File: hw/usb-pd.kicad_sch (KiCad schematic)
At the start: 16 parts, among them J2101 USB C power only, Q2101 SQJ433EP, U2103 STUSB4500QTR

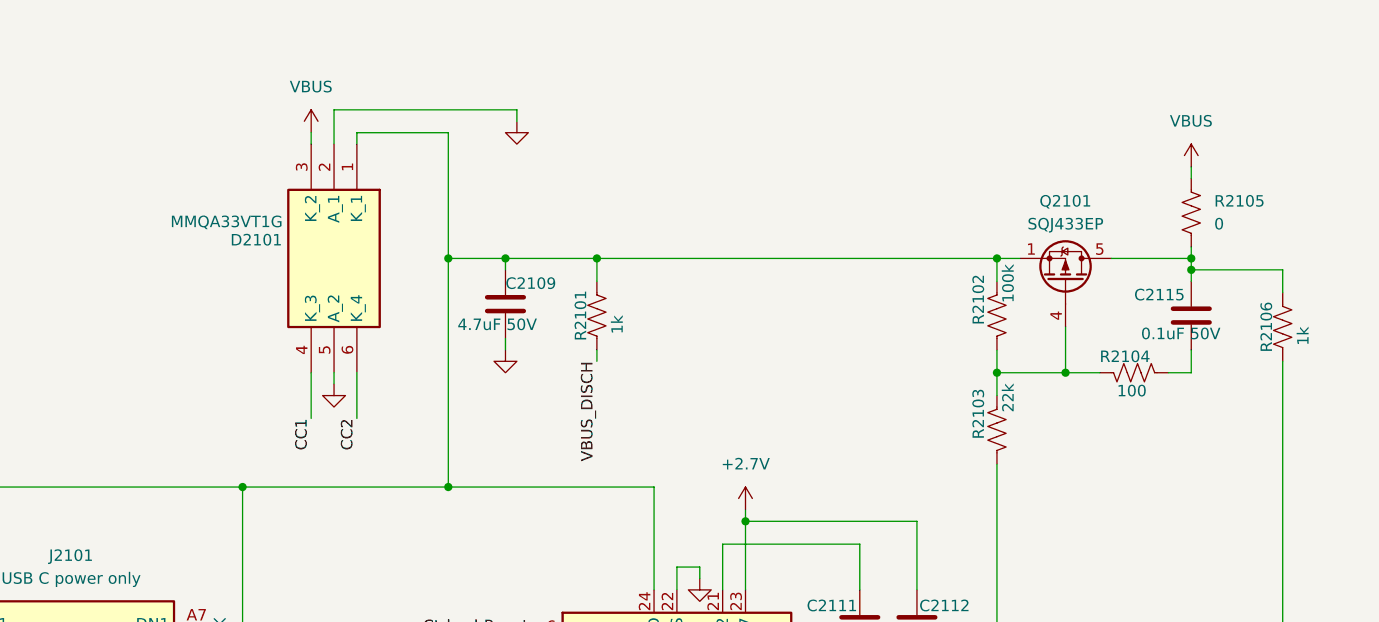
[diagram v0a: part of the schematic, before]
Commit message: I laid down three QSDs but have not done any canyon for 800 ohm yet. Starting to look at Veer buck/boost to round out my understanding.
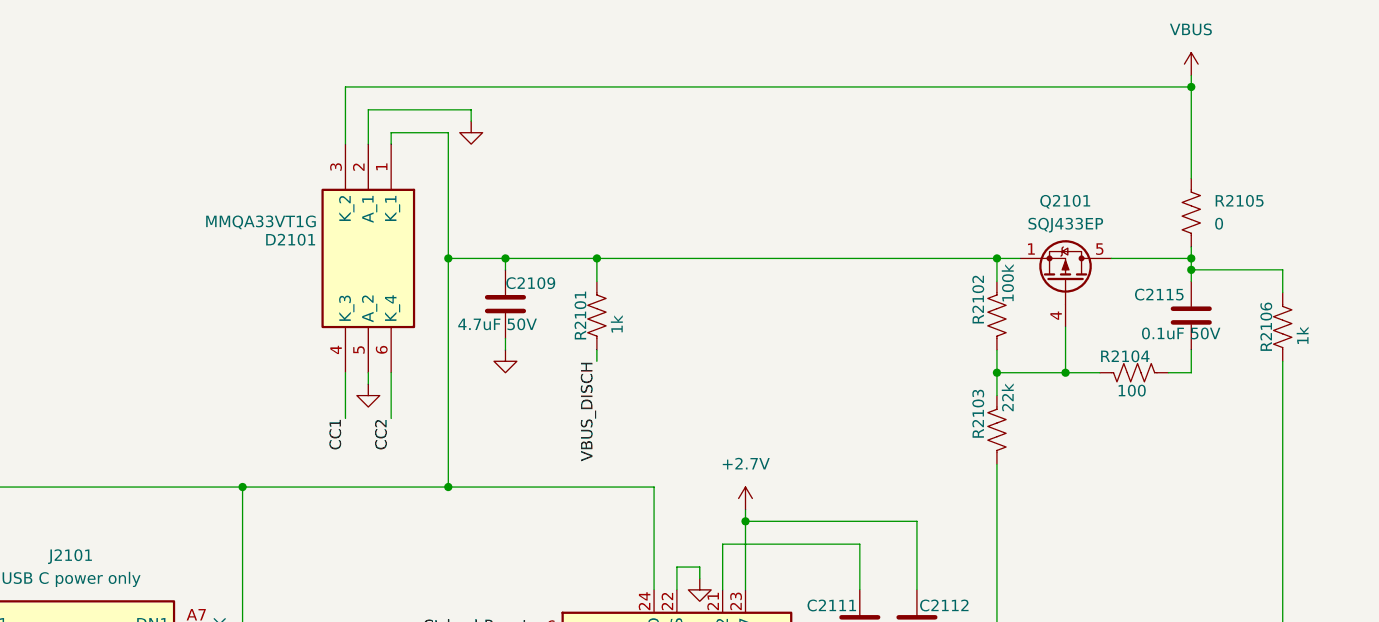
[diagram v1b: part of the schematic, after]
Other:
- moved on the sheet: D2101

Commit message: Giant rename to actual NexRig project name which seems to have stuck
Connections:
- net at C2115.1, Q2101.5 (D), R2105.2: now also R2106.2; no longer R2106.1
- net at U2103.9 (DISCH): now also R2106.1; no longer R2106.2
- net +3.3V renamed +3.3V-ON
- net VBUS renamed VUSBPD
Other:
- moved on the sheet: C2115, Q2101, R2102, R2103, R2104, R2105, R2106, R2107, R2108

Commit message: Schematic capture of the USBPD and +12V (+12V has priority) power scheme is "done". Have started working on RF deck mezzanine module but not yet divorced into another project
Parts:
- C7935: renamed from C2115; value 0.1uF 50V -> 100nF 50V
- renumbered C2109 to C7929, C2111 to C7931, C2112 to C7932, D2101 to D7705, J2101 to J7706, Q2101 to Q7705, R2101 to R7837, R2102 to R7838, R2103 to R7839, R2106 to R7840, R2104 to R7841, R2105 to R7842, R2107 to R7843, R2108 to R7844, U2103 to U7765

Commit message: Last rites for 800 ohm rx preselector, and probably the RF deck which was stillborn
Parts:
- renumbered C7929 to C7908, C7931 to C7910, C7932 to C7911, C7935 to C7914, R7837 to R7814, R7838 to R7815, R7839 to R7816, R7840 to R7817, R7841 to R7818, R7842 to R7819, R7843 to R7820, R7844 to R7821, U7765 to U7743
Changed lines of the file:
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@@
 	(title_block
 		(title "USB-PD")
-		(date "2025-10-28")
+		(date "2025-10-13")
 		(company "WB7NAB")
 		(comment 1 "Alan Mimms")

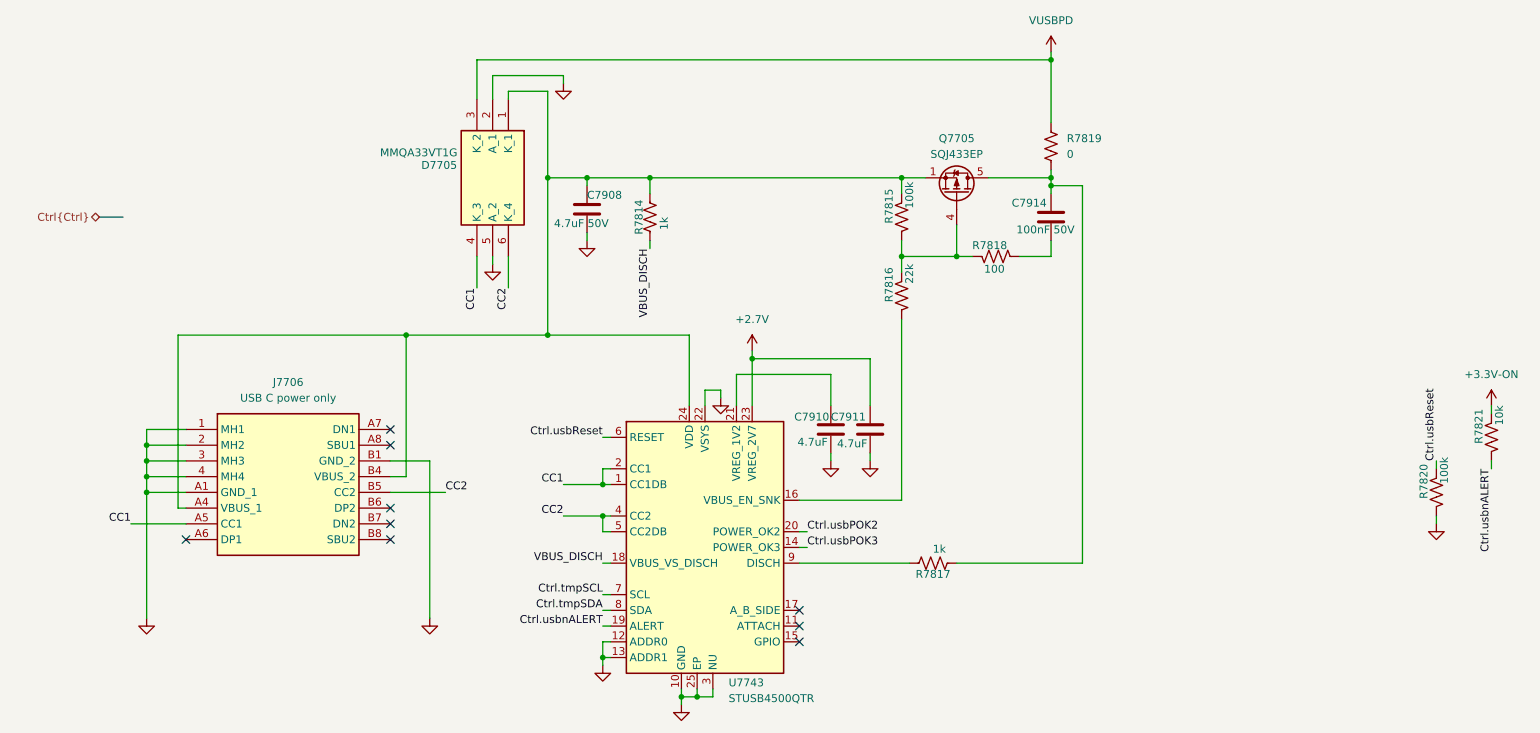
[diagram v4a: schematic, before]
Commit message: Fixed GPIO assignments. Fixed symbol for GRL2-2 relays.
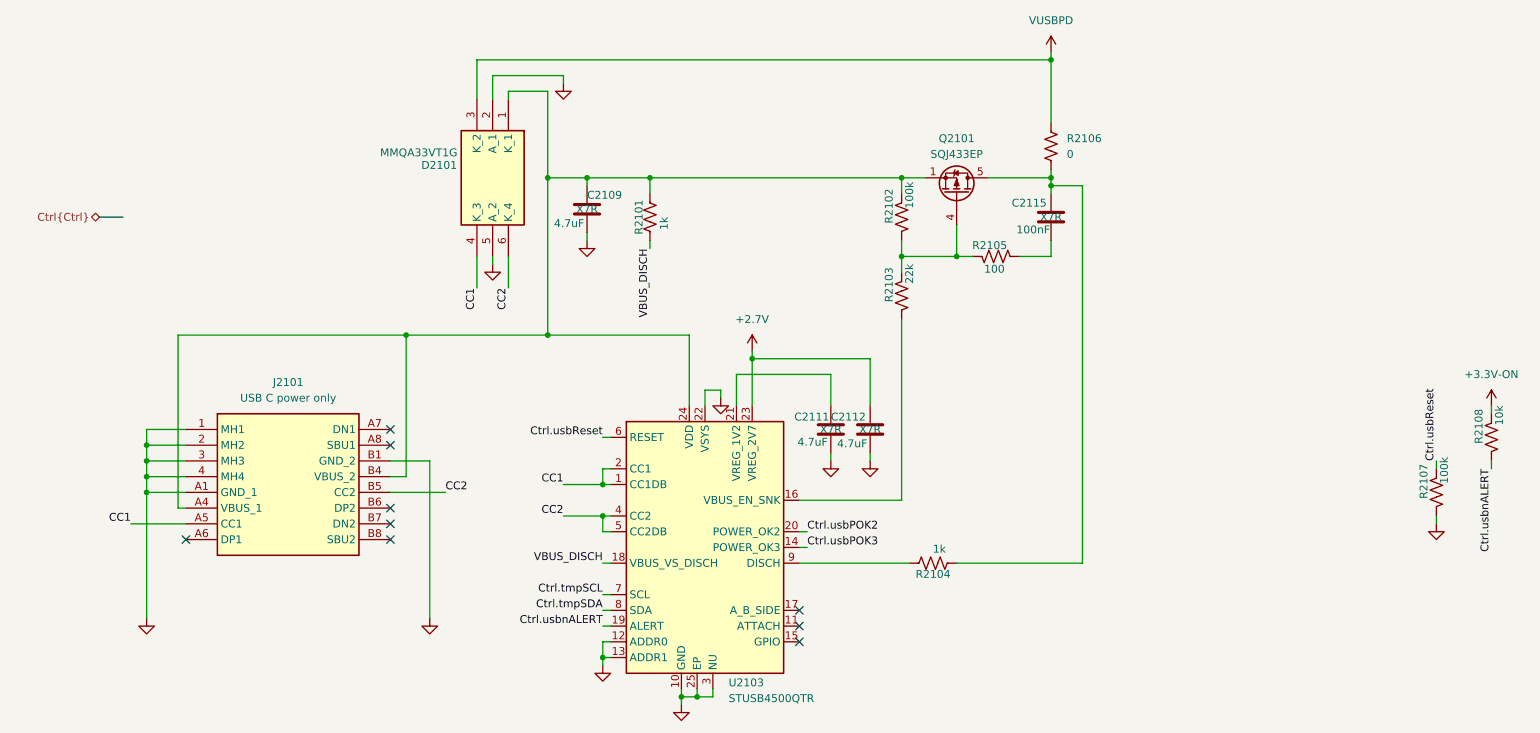
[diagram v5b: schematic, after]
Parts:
- C2109: renamed from C7908; value 4.7uF 50V -> 4.7uF; cap-type (none) -> X7R; working-voltage (none) -> 50V
- C2111: renamed from C7910; cap-type (none) -> X7R; working-voltage (none) -> 10V
- C2112: renamed from C7911; cap-type (none) -> X7R; working-voltage (none) -> 10V
- C2115: renamed from C7914; value 100nF 50V -> 100nF; cap-type (none) -> X7R; working-voltage (none) -> 50V
- renumbered D7705 to D2101, J7706 to J2101, Q7705 to Q2101, R7814 to R2101, R7815 to R2102, R7816 to R2103, R7817 to R2104, R7818 to R2105, R7819 to R2106, R7820 to R2107, R7821 to R2108, U7743 to U2103

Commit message: I think I have finished the relay conversion and 5V SPI I/O expander crap
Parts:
- renumbered C2109 to C7944, C2111 to C7947, C2112 to C7948, C2115 to C7950, D2101 to D7725, J2101 to J7706, Q2101 to Q7705, R2101 to R7829, R2102 to R7830, R2103 to R7831, R2104 to R7832, R2105 to R7833, R2106 to R7834, R2107 to R7835, R2108 to R7836, U2103 to U7754

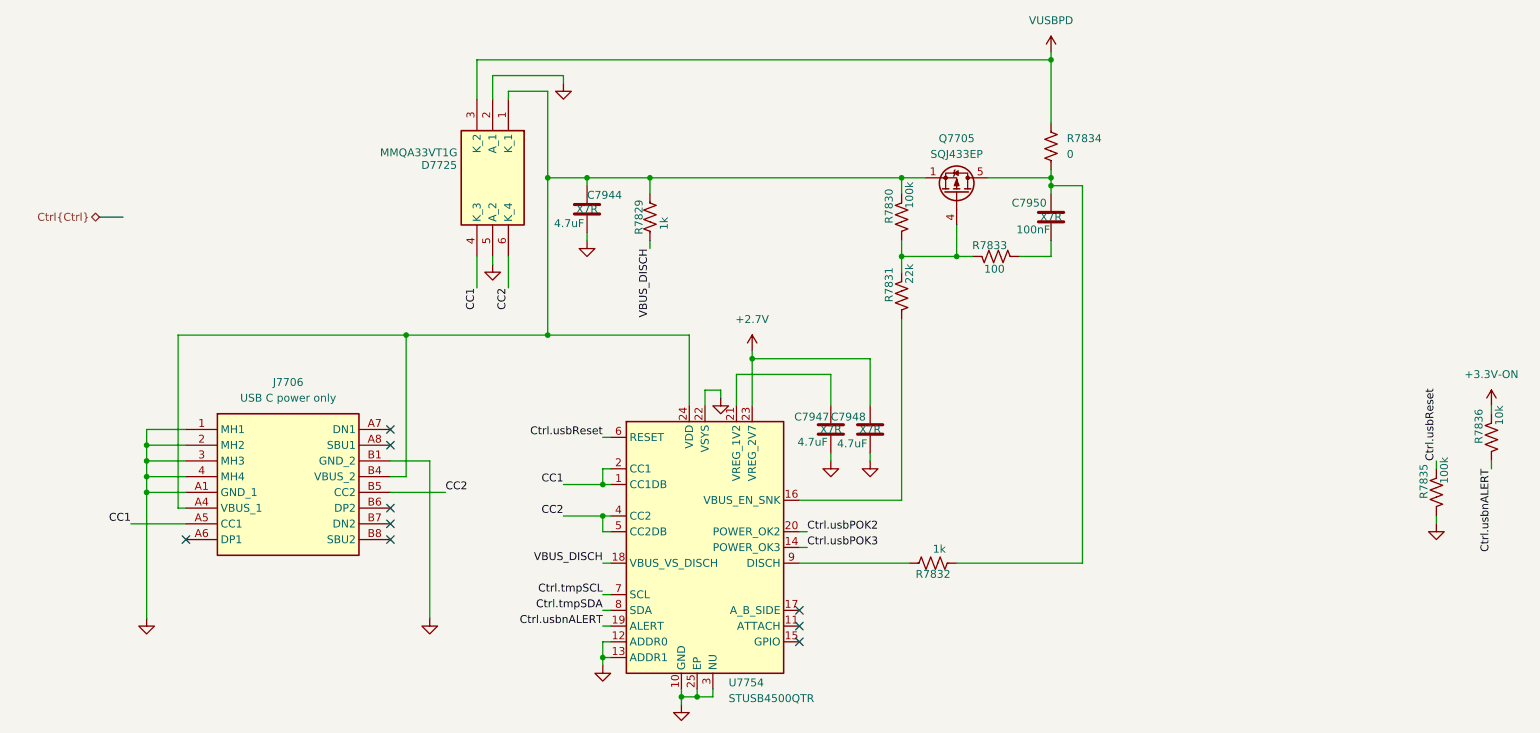
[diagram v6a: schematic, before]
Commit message: Starting to build guanella transformers. Mostly converted to 1-2-1 tx, but FPGA still to do.
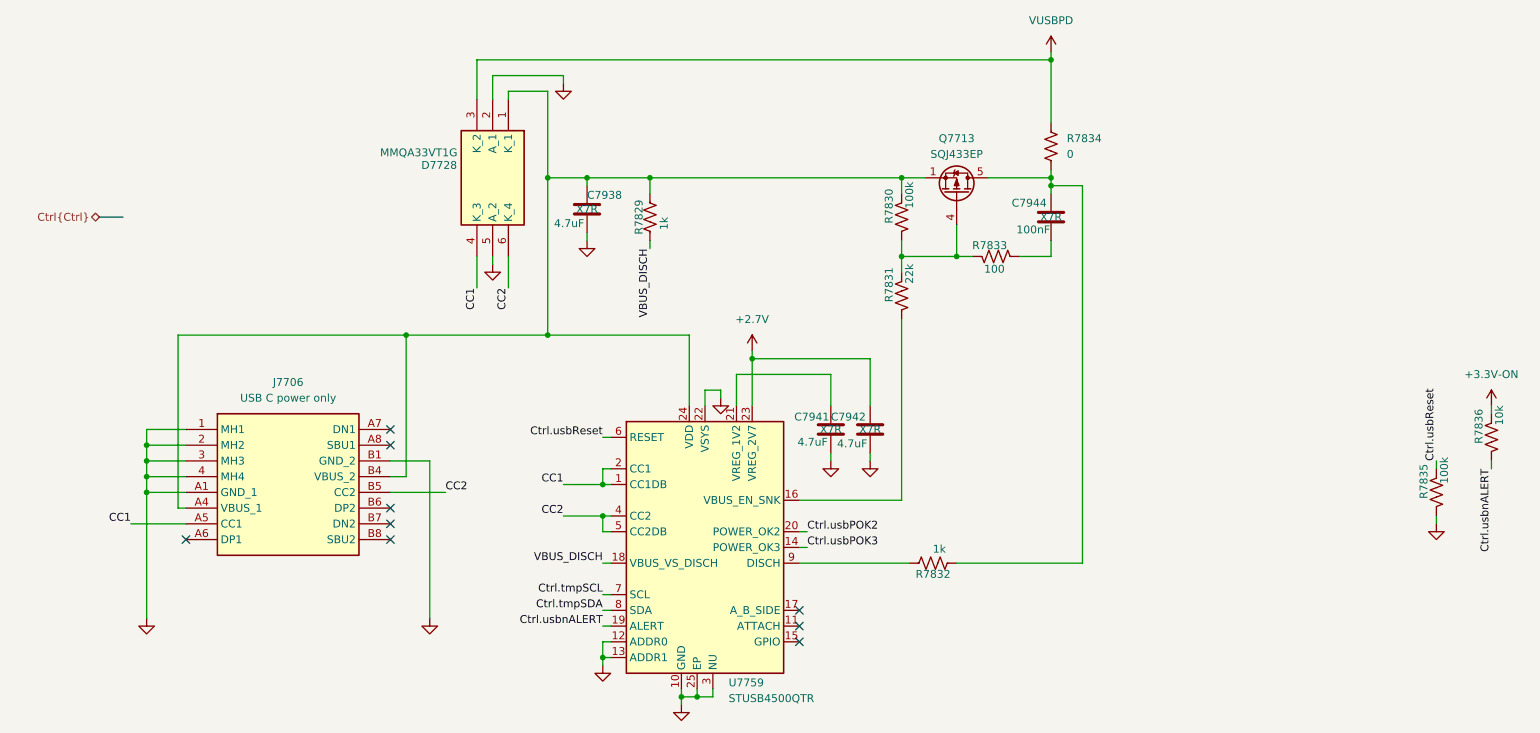
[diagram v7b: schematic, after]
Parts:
- renumbered C7944 to C7938, C7947 to C7941, C7948 to C7942, C7950 to C7944, D7725 to D7728, Q7705 to Q7713, U7754 to U7759

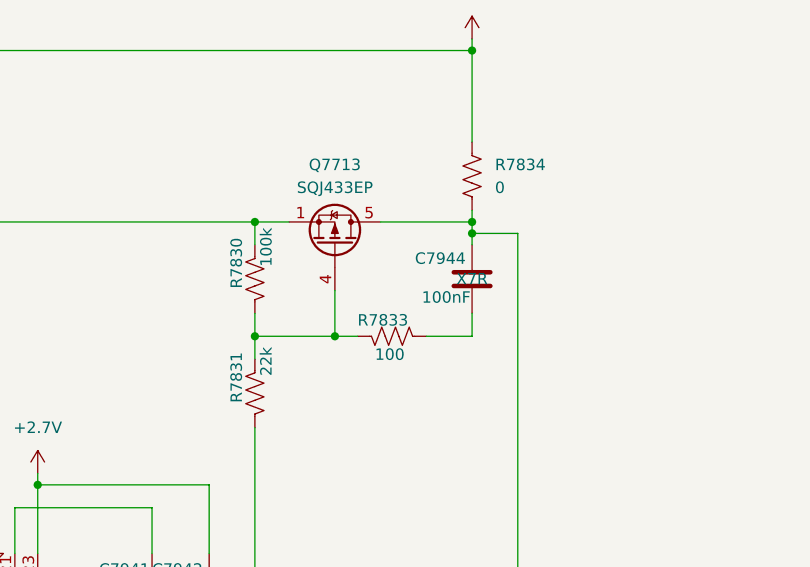
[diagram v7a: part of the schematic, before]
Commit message: Checkpoint. FPGA is mostly done (need a check!). Working on new LPFs. Need inductor footprints and to fix a bunch of broken/missing footprints.
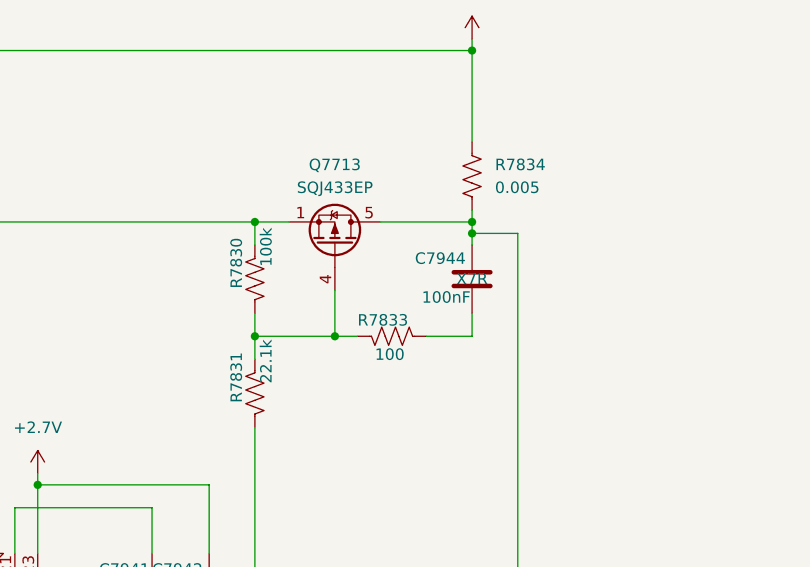
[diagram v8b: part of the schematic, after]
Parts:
- C7944: footprint Capacitor_SMD:C_1206_3216Metric -> Capacitor_SMD:C_0603_1608Metric
- R7830, R7835, R7836: footprint Resistor_SMD:R_0603_1608Metric -> Resistor_SMD:R_0402_1005Metric
- R7831: value 22k -> 22.1k
- R7834: value 0 -> 0.005; footprint Resistor_SMD:R_1206_3216Metric -> Resistor_SMD:R_0612_1632Metric
